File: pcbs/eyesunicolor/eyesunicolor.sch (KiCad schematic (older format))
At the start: 43 parts, among them J1 SUPP28, J2 SUPP28, P1 CONN_5X2, P2 CONN_5X2, P3 CONN_5X2

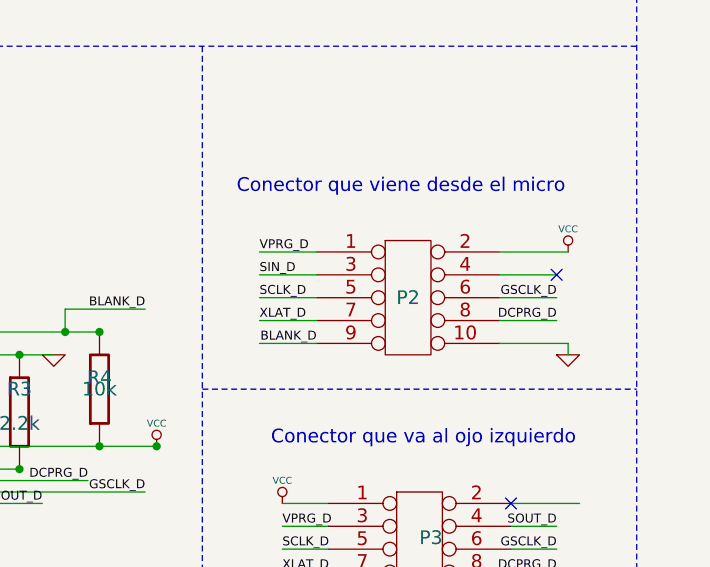
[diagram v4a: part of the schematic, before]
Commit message: Intente terminar los ojos, pero no puedo co el ojo derecho. TERMINAR URGENTE
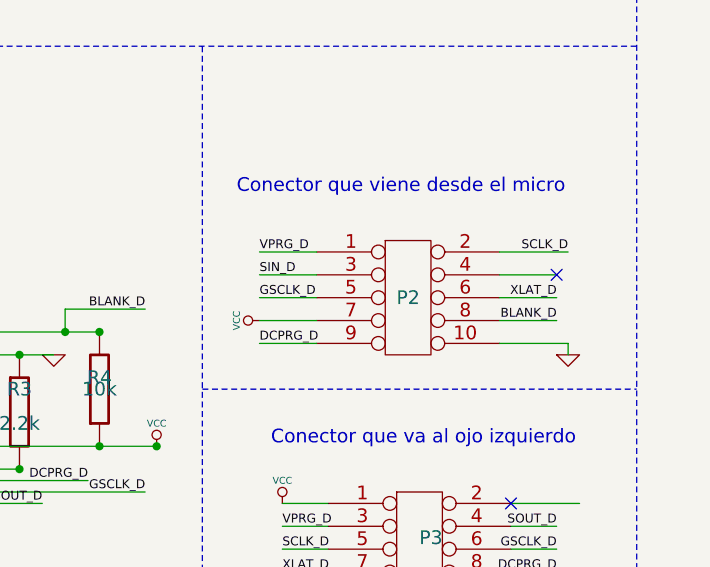
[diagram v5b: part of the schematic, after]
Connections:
- net BLANK_D: now also P2.8; no longer P2.9
- net DCPRG_D: now also P2.9; no longer P2.8
- net GSCLK_D: now also P2.5; no longer P2.6
- net SCLK_D: now also P2.2; no longer P2.5
- net VCC: now also P2.7; no longer P2.2
- net XLAT_D: now also P2.6; no longer P2.7
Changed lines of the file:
@@
-EESchema Schematic File Version 2  date Fri 25 Oct 2013 21:43:28 ART
+EESchema Schematic File Version 2  date Fri 08 Nov 2013 21:30:37 ART
 LIBS:power
 LIBS:device
@@
 Sheet 1 1
 Title ""
-Date "26 oct 2013"
+Date "9 nov 2013"
 Rev ""
 Comp ""
@@
 Text Label 8600 4600 0    39   ~ 0
 SIN_D
+Text Label 9950 4500 2    39   ~ 0
+SCLK_D
+Text Label 9900 4700 2    39   ~ 0
+XLAT_D
+Text Label 9900 4800 2    39   ~ 0
+BLANK_D
+Text Label 8600 4900 0    39   ~ 0
+DCPRG_D
 Text Label 8600 4700 0    39   ~ 0
-SCLK_D
-Text Label 8600 4800 0    39   ~ 0
-XLAT_D
-Text Label 8850 4900 2    39   ~ 0
-BLANK_D
-Text Label 9900 4800 2    39   ~ 0
-DCPRG_D
-Text Label 9900 4700 2    39   ~ 0
 GSCLK_D
 $Comp
@@
 L VCC #PWR09
 U 1 1 5261D2DF
-P 9950 4500
-F 0 "#PWR09" H 10000 4550 60  0001 C CNN
-F 1 "VCC" H 9950 4500 60  0001 C CNN
-F 2 "" H 9950 4500 60  0001 C CNN
-F 3 "" H 9950 4500 60  0000 C CNN
-F 4 "#PWR" H 9950 4600 30  0001 C CNN "Reference"
-F 5 "VCC" H 9950 4600 30  0000 C CNN "Value"
-F 6 "" H 9950 4500 60  0000 C CNN "Footprint"
-	1    9950 4500
-	1    0    0    -1
-$EndComp
-$Comp
+P 8600 4800
+F 0 "#PWR09" H 8650 4850 60  0001 C CNN
+F 1 "VCC" H 8600 4800 60  0001 C CNN
+F 2 "" H 8600 4800 60  0001 C CNN
+F 3 "" H 8600 4800 60  0000 C CNN
+F 4 "#PWR" H 8600 4900 30  0001 C CNN "Reference"
+F 5 "VCC" H 8600 4900 30  0000 C CNN "Value"
+F 6 "" H 8600 4800 60  0000 C CNN "Footprint"
+	1    8600 4800
+	0    -1   -1   0
+$EndComp
+$Comp

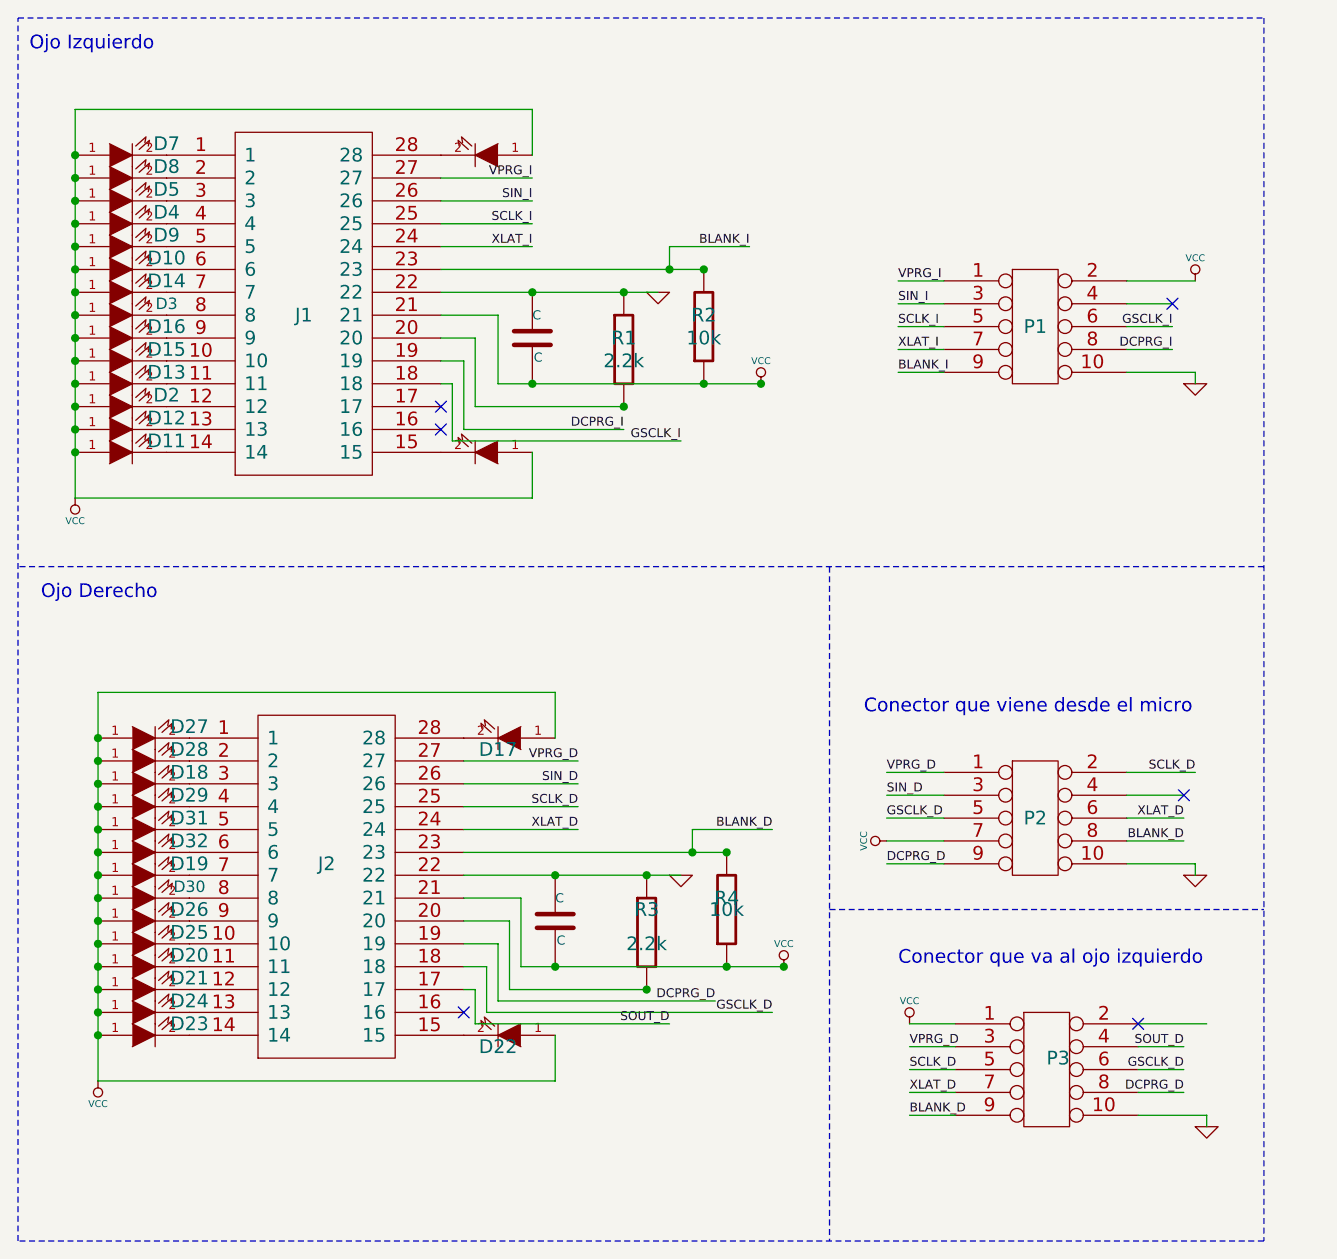
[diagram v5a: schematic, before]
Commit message: Elimino archivos de backup y actualizo pcb y schm
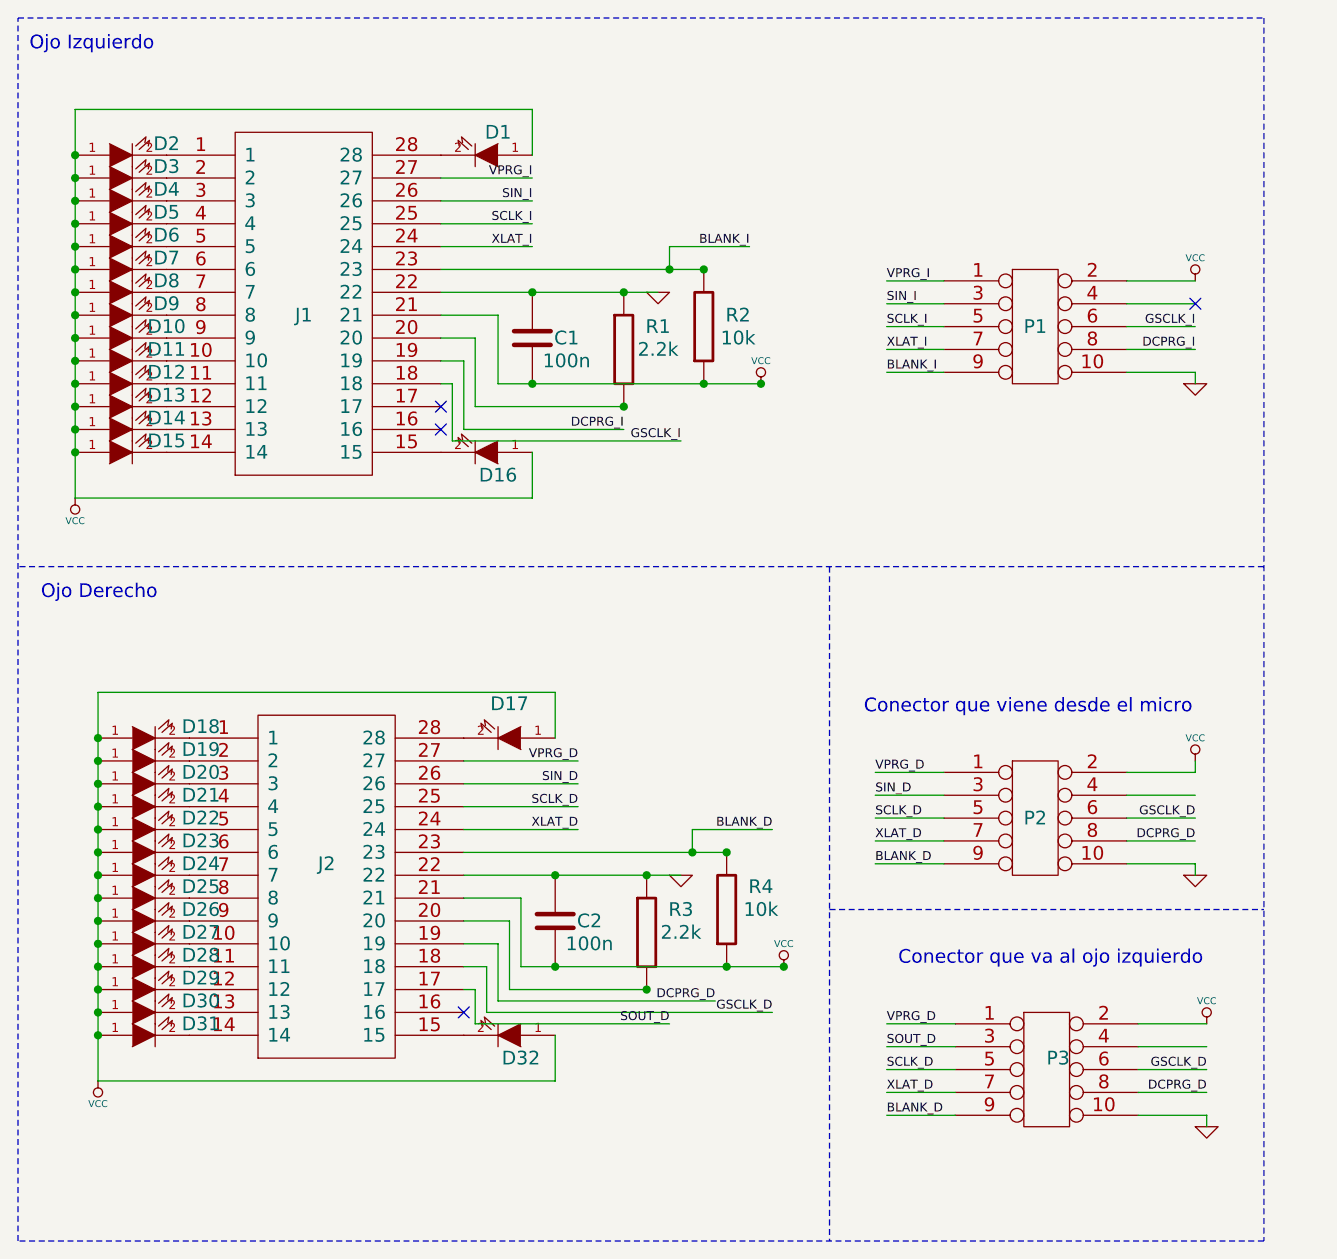
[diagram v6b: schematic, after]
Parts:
- C1, C2: value C -> 100n; Reference C -> (none); Value C -> (none)
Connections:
- net BLANK_D: now also P2.9; no longer P2.8
- net DCPRG_D: now also P2.8; no longer P2.9
- net GSCLK_D: now also P2.6; no longer P2.5
- net SCLK_D: now also P2.5; no longer P2.2
- net SOUT_D: now also P3.3; no longer P3.4
- net VCC: now also P2.2, P3.2; no longer P2.7, P3.1
- net VPRG_D: now also P3.1; no longer P3.3
- net XLAT_D: now also P2.7; no longer P2.6
- net at J1.1: now also D2.2 (K); no longer D7.2 (K)
- net at J1.10: now also D11.2 (K); no longer D15.2 (K)
- net at J1.11: now also D12.2 (K); no longer D13.2 (K)
- net at J1.12: now also D13.2 (K); no longer D2.2 (K)
- net at J1.13: now also D14.2 (K); no longer D12.2 (K)
- net at J1.14: now also D15.2 (K); no longer D11.2 (K)
- net at J1.15: now also D16.2 (K); no longer D1.2 (K)
- net at J1.2: now also D3.2 (K); no longer D8.2 (K)
- net at J1.28: now also D1.2 (K); no longer D6.2 (K)
- net at J1.3: now also D4.2 (K); no longer D5.2 (K)
- net at J1.4: now also D5.2 (K); no longer D4.2 (K)
- net at J1.5: now also D6.2 (K); no longer D9.2 (K)
- net at J1.6: now also D7.2 (K); no longer D10.2 (K)
- net at J1.7: now also D8.2 (K); no longer D14.2 (K)
- net at J1.8: now also D9.2 (K); no longer D3.2 (K)
- net at J1.9: now also D10.2 (K); no longer D16.2 (K)
- net at J2.1: now also D18.2 (K); no longer D27.2 (K)
- net at J2.10: now also D27.2 (K); no longer D25.2 (K)
- net at J2.11: now also D28.2 (K); no longer D20.2 (K)
- net at J2.12: now also D29.2 (K); no longer D21.2 (K)
- net at J2.13: now also D30.2 (K); no longer D24.2 (K)
- net at J2.14: now also D31.2 (K); no longer D23.2 (K)
- net at J2.15: now also D32.2 (K); no longer D22.2 (K)
- net at J2.2: now also D19.2 (K); no longer D28.2 (K)
- net at J2.3: now also D20.2 (K); no longer D18.2 (K)
- net at J2.4: now also D21.2 (K); no longer D29.2 (K)
- net at J2.5: now also D22.2 (K); no longer D31.2 (K)
- net at J2.6: now also D23.2 (K); no longer D32.2 (K)
- net at J2.7: now also D24.2 (K); no longer D19.2 (K)
- net at J2.8: now also D25.2 (K); no longer D30.2 (K)
- no-connect marks 6 -> 4
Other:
- moved on the sheet: D10, D11, D12, D13, D14, D15, D16, D18, D19, D2, D20, D21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
